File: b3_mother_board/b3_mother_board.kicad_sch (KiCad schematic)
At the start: 23 parts, among them J1 Drawbars_1, J2 Drawbars_3, J3 Conn_01x03, J4 Drawbars_2, J5 Drawbars_4, J6 Conn_01x03, J7 To Vibrato/Chorus Rotary Knob, J8 To Overdrive/Vibrato PCB, J9 To Percussions PCB, SW1 SW_Push

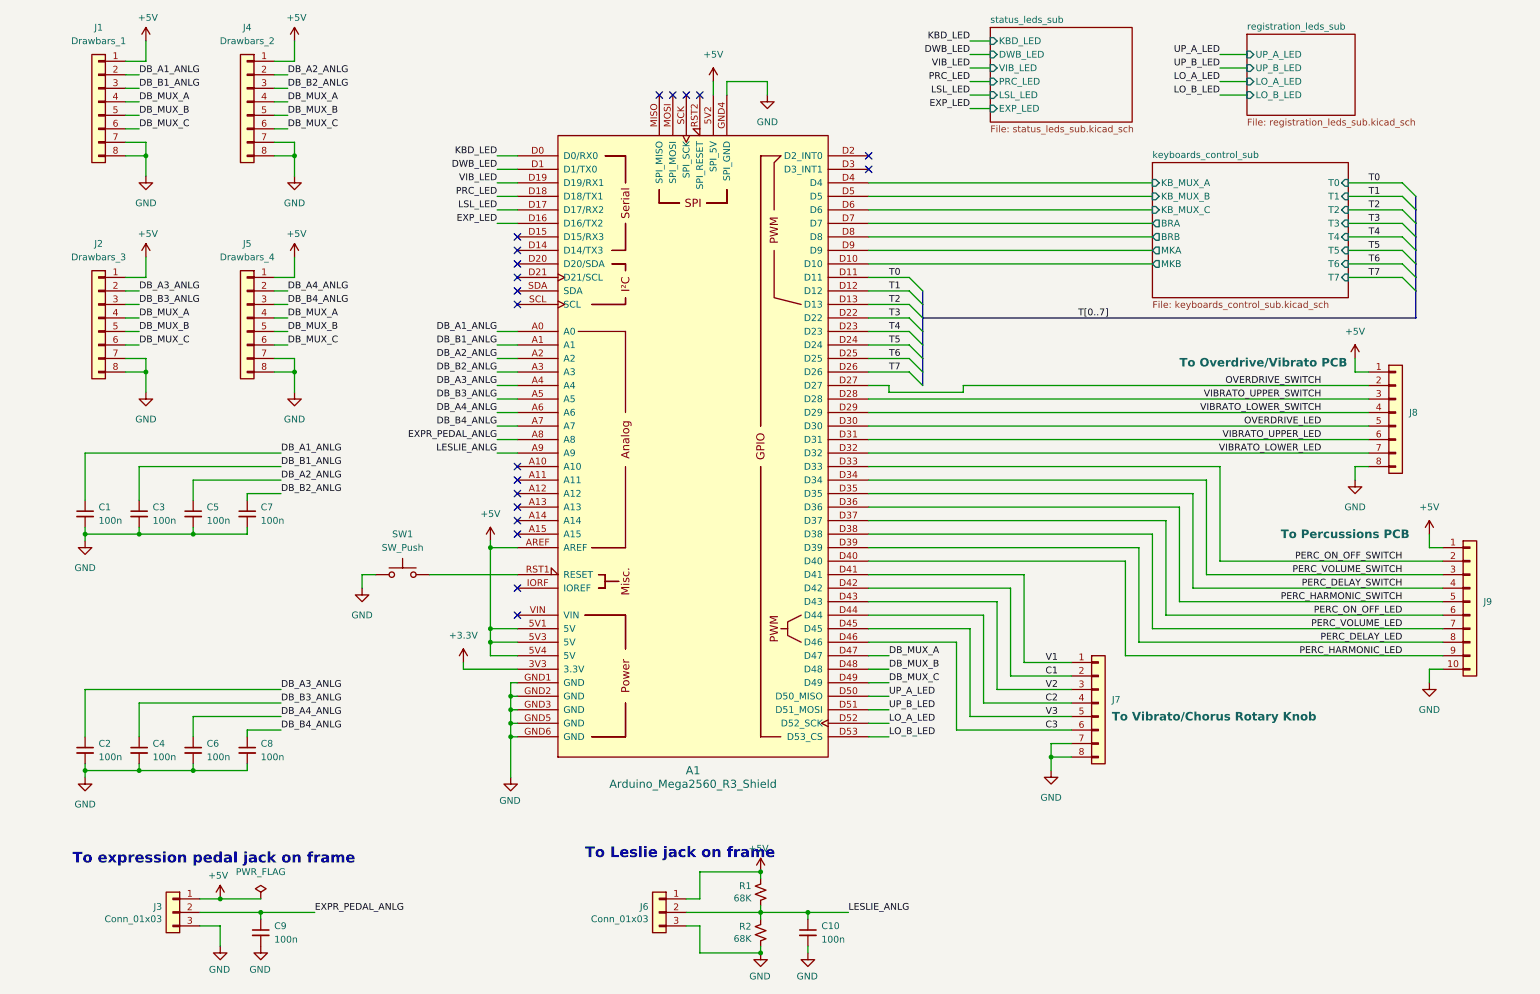
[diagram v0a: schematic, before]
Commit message: New organ architecture with mother board
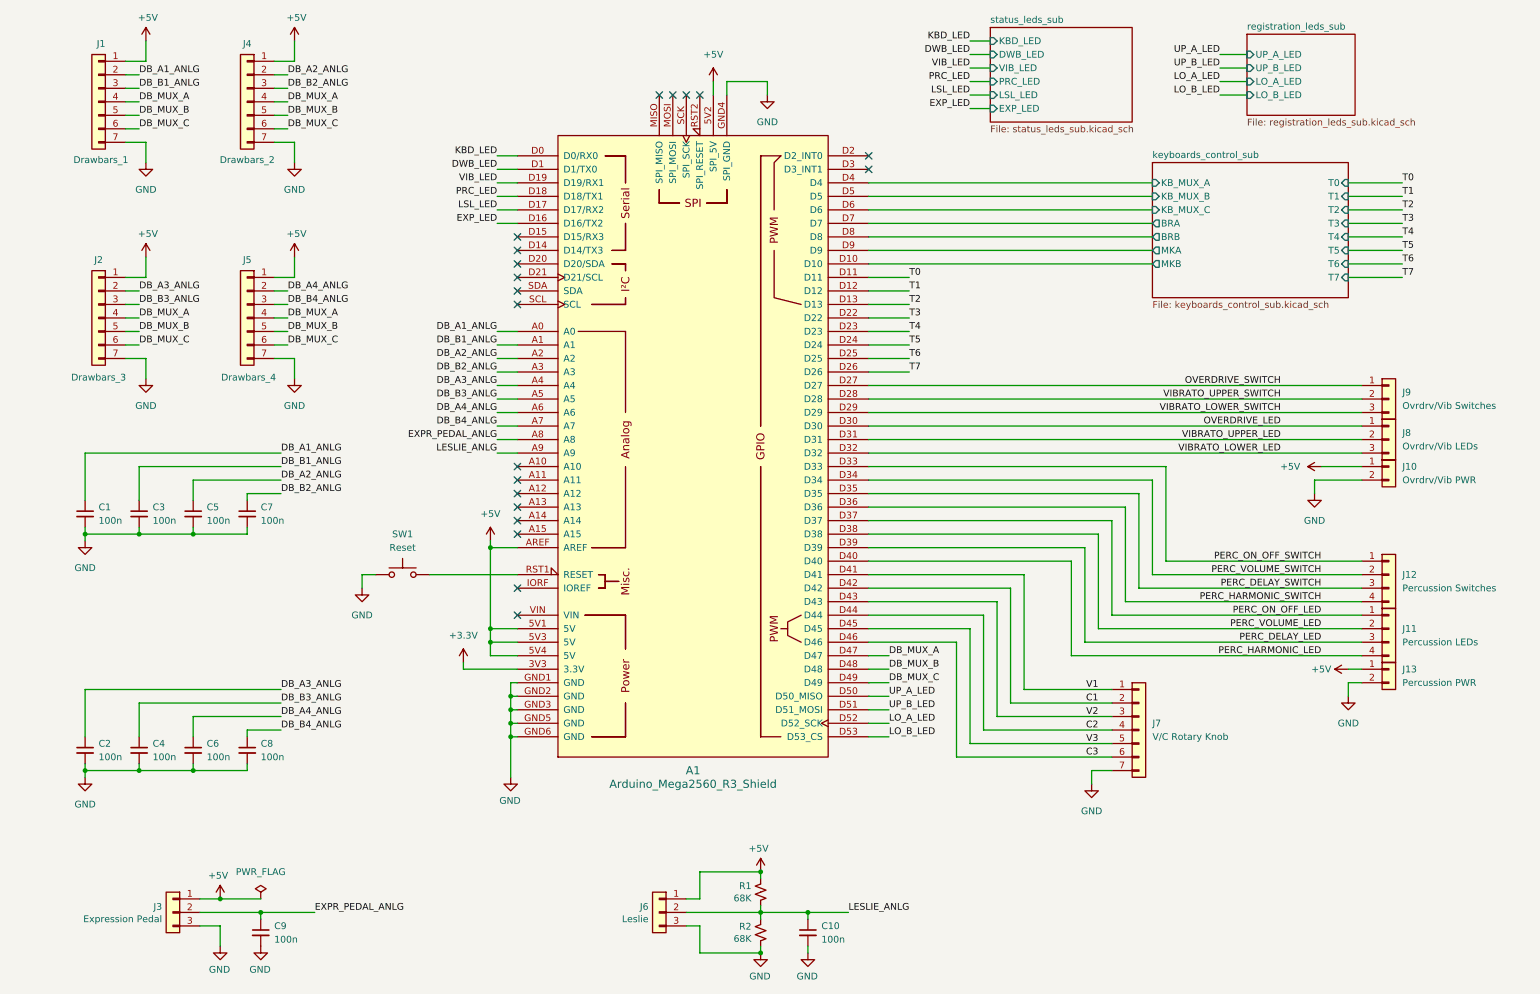
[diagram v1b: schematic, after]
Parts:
- removed J1: Drawbars_1, symbol Connector_Generic:Conn_01x08
- removed J8: To Overdrive/Vibrato PCB, symbol Connector_Generic:Conn_01x08
- removed J9: To Percussions PCB, symbol Connector_Generic:Conn_01x10
- added J1: Drawbars_1, Connector_JST:JST_XH_B7B-XH-A_1x07_P2.50mm_Vertical, symbol Connector_Generic:Conn_01x07
- added J10: Ovrdrv/Vib PWR, Connector_JST:JST_XH_B2B-XH-A_1x02_P2.50mm_Vertical, symbol Connector_Generic:Conn_01x02
- added J11: Percussion LEDs, Connector_JST:JST_XH_B4B-XH-A_1x04_P2.50mm_Vertical, symbol Connector_Generic:Conn_01x04
- added J12: Percussion Switches, Connector_JST:JST_XH_B4B-XH-A_1x04_P2.50mm_Vertical, symbol Connector_Generic:Conn_01x04
- added J13: Percussion PWR, Connector_JST:JST_XH_B2B-XH-A_1x02_P2.50mm_Vertical, symbol Connector_Generic:Conn_01x02
- added J8: Ovrdrv/Vib LEDs, Connector_JST:JST_XH_B3B-XH-A_1x03_P2.50mm_Vertical, symbol Connector_Generic:Conn_01x03
- added J9: Ovrdrv/Vib Switches, Connector_JST:JST_XH_B3B-XH-A_1x03_P2.50mm_Vertical, symbol Connector_Generic:Conn_01x03
- C1, C10, C2, C3, C4, C5, C6, C7, C8, C9: footprint (none) -> Capacitor_THT:C_Rect_L11.5mm_W4.3mm_P10.00mm_MKT
- J2, J4, J5: footprint (none) -> Connector_JST:JST_XH_B7B-XH-A_1x07_P2.50mm_Vertical; symbol Connector_Generic:Conn_01x08 -> Connector_Generic:Conn_01x07
- J3: value Conn_01x03 -> Expression Pedal; footprint Connector_PinHeader_2.54mm:PinHeader_1x03_P2.54mm_Vertical -> Connector_JST:JST_XH_B3B-XH-A_1x03_P2.50mm_Vertical
- J6: value Conn_01x03 -> Leslie; footprint Connector_PinHeader_2.54mm:PinHeader_1x03_P2.54mm_Vertical -> Connector_JST:JST_XH_B3B-XH-A_1x03_P2.50mm_Vertical
- J7: value To Vibrato/Chorus Rotary Knob -> V/C Rotary Knob; footprint (none) -> Connector_JST:JST_XH_B7B-XH-A_1x07_P2.50mm_Vertical; symbol Connector_Generic:Conn_01x08 -> Connector_Generic:Conn_01x07
- R1, R2: footprint Resistor_SMD:R_1206_3216Metric_Pad1.30x1.75mm_HandSolder -> Resistor_THT:R_Axial_DIN0207_L6.3mm_D2.5mm_P7.62mm_Horizontal
- SW1: value SW_Push -> Reset; footprint (none) -> Button_Switch_THT:SW_PUSH_6mm_H4.3mm
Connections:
- net +5V: now also J1.1 (Pin_1), J10.1 (Pin_1), J13.1 (Pin_1)
- net DB_A1_ANLG: now also J1.2 (Pin_2)
- net DB_B1_ANLG: now also J1.3 (Pin_3)
- net DB_MUX_A: now also J1.4 (Pin_4)
- net DB_MUX_B: now also J1.5 (Pin_5)
- net DB_MUX_C: now also J1.6 (Pin_6)
- net GND: now also J1.7 (Pin_7), J10.2 (Pin_2), J13.2 (Pin_2); no longer J2.8 (Pin_8), J4.8 (Pin_8), J5.8 (Pin_8), J7.8 (Pin_8)
- net OVERDRIVE_LED: now also J8.1 (Pin_1)
- net OVERDRIVE_SWITCH: now also J9.1 (Pin_1)
- net PERC_DELAY_LED: now also J11.3 (Pin_3)
- net PERC_DELAY_SWITCH: now also J12.3 (Pin_3)
- net PERC_HARMONIC_LED: now also J11.4 (Pin_4)
- net PERC_HARMONIC_SWITCH: now also J12.4 (Pin_4)
- net PERC_ON_OFF_LED: now also J11.1 (Pin_1)
- net PERC_ON_OFF_SWITCH: now also J12.1 (Pin_1)
- net PERC_VOLUME_LED: now also J11.2 (Pin_2)
- net PERC_VOLUME_SWITCH: now also J12.2 (Pin_2)
- net VIBRATO_LOWER_LED: now also J8.3 (Pin_3)
- net VIBRATO_LOWER_SWITCH: now also J9.3 (Pin_3)
- net VIBRATO_UPPER_LED: now also J8.2 (Pin_2)
- net VIBRATO_UPPER_SWITCH: now also J9.2 (Pin_2)
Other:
- note removed: "To Leslie jack on frame"
- note removed: "To expression pedal jack on frame"
